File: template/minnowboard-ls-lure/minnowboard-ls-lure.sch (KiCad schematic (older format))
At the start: 1 part, among them P1 CONN_02X13

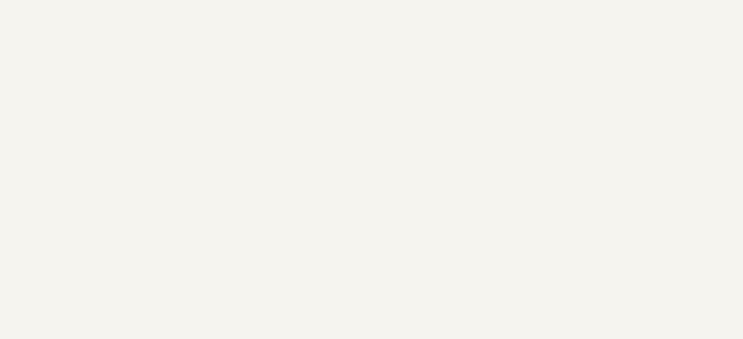
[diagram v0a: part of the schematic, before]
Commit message: Add new mounting hole symbols to schematic
Signed-off-by: Michael Welling <mwelling@ieee.org>
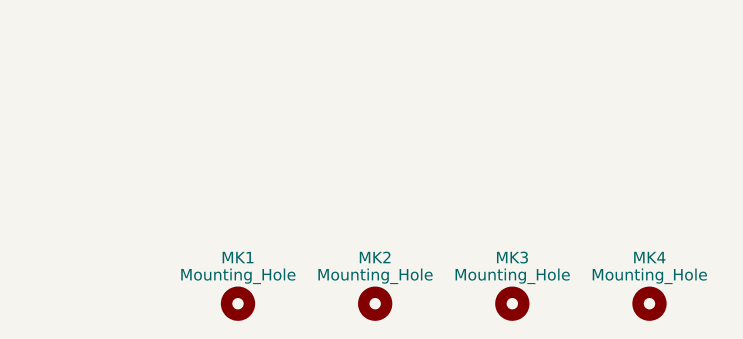
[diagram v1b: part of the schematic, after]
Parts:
- added MK1, MK2, MK3, MK4: Mounting_Hole, Mounting_Holes:MountingHole_3-5mm, symbol Mounting_Hole
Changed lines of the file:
@@
 LIBS:contrib
 LIBS:valves
+LIBS:mechanical
 LIBS:minnowboard-ls-lure-cache
 EELAYER 25 0
@@
 $EndComp
 $Comp
-L GND #PWR?
+L GND #PWR3
 U 1 1 576DC243
 P 2950 3000
-F 0 "#PWR?" H 2950 2750 50  0001 C CNN
+F 0 "#PWR3" H 2950 2750 50  0001 C CNN
 F 1 "GND" H 2950 2850 50  0000 C CNN
 F 2 "" H 2950 3000 50  0000 C CNN
@@
 $EndComp
 $Comp
-L GND #PWR?
+L GND #PWR2
 U 1 1 576DC271
 P 2250 3000
-F 0 "#PWR?" H 2250 2750 50  0001 C CNN
+F 0 "#PWR2" H 2250 2750 50  0001 C CNN
 F 1 "GND" H 2250 2850 50  0000 C CNN
 F 2 "" H 2250 3000 50  0000 C CNN
@@
 $EndComp
 $Comp
-L +3.3V #PWR?
+L +3.3V #PWR4
 U 1 1 576DC2D3
 P 3050 1650
-F 0 "#PWR?" H 3050 1500 50  0001 C CNN
+F 0 "#PWR4" H 3050 1500 50  0001 C CNN
 F 1 "+3.3V" H 3050 1790 50  0000 C CNN
 F 2 "" H 3050 1650 50  0000 C CNN
@@
 $EndComp
 $Comp
-L +5V #PWR?
+L +5V #PWR1
 U 1 1 576DC2E9
 P 2150 1650
-F 0 "#PWR?" H 2150 1500 50  0001 C CNN
+F 0 "#PWR1" H 2150 1500 50  0001 C CNN
 F 1 "+5V" H 2150 1790 50  0000 C CNN
 F 2 "" H 2150 1650 50  0000 C CNN
@@
 Wire Wire Line
 	2150 1850 2350 1850
+$Comp
+L Mounting_Hole MK2
+U 1 1 58633372
+P 5350 7500
+F 0 "MK2" H 5350 7700 50  0000 C CNN
+F 1 "Mounting_Hole" H 5350 7625 50  0000 C CNN
+F 2 "Mounting_Holes:MountingHole_3-5mm" H 5350 7500 60  0001 C CNN
+F 3 "" H 5350 7500 60  0001 C CNN
+	1    5350 7500
+	1    0    0    -1
+$EndComp
+$Comp
+L Mounting_Hole MK1
+U 1 1 58633409
+P 4750 7500
+F 0 "MK1" H 4750 7700 50  0000 C CNN
+F 1 "Mounting_Hole" H 4750 7625 50  0000 C CNN
+F 2 "Mounting_Holes:MountingHole_3-5mm" H 4750 7500 60  0001 C CNN
+F 3 "" H 4750 7500 60  0001 C CNN
+	1    4750 7500
+	1    0    0    -1
+$EndComp
+$Comp
+L Mounting_Hole MK3
+U 1 1 58633454
+P 5950 7500
+F 0 "MK3" H 5950 7700 50  0000 C CNN
+F 1 "Mounting_Hole" H 5950 7625 50  0000 C CNN
+F 2 "Mounting_Holes:MountingHole_3-5mm" H 5950 7500 60  0001 C CNN
+F 3 "" H 5950 7500 60  0001 C CNN
+	1    5950 7500
+	1    0    0    -1
+$EndComp
+$Comp
+L Mounting_Hole MK4
+U 1 1 5863348E
+P 6550 7500
+F 0 "MK4" H 6550 7700 50  0000 C CNN
+F 1 "Mounting_Hole" H 6550 7625 50  0000 C CNN
+F 2 "Mounting_Holes:MountingHole_3-5mm" H 6550 7500 60  0001 C CNN
+F 3 "" H 6550 7500 60  0001 C CNN
+	1    6550 7500
+	1    0    0    -1
+$EndComp
 $EndSCHEMATC
